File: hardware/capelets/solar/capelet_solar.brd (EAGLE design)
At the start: 54.6 x 40.5 mm, 4 parts

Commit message: hardware: updated capelets
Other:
- board text added: "SHEPHERD v1.4 CAPELET SOLAR"
- board text removed: "+"
- board text removed: "-"
- board text removed: "SHEPHERD v1.3 CAPELET SOLAR"
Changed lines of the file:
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@@
 <?xml version="1.0" encoding="utf-8"?>
 <!DOCTYPE eagle SYSTEM "eagle.dtd">
-<eagle version="9.3.2">
+<eagle version="9.4.2">
 <drawing>
 <settings>
@@
 <board>
 <plain>
-<text x="9.398" y="43.053" size="1.778" layer="25" font="vector" ratio="15">SHEPHERD v1.3 CAPELET SOLAR</text>
-<text x="9.652" y="1.27" size="1.778" layer="25" font="vector" ratio="15">+</text>
-<text x="4.572" y="1.397" size="1.778" layer="25" font="vector" ratio="15">-</text>
+<text x="8.001" y="42.418" size="1.905" layer="29" font="vector" ratio="17">SHEPHERD v1.4 CAPELET SOLAR</text>
 <dimension x1="0" y1="45.847" x2="54.61" y2="45.847" x3="27.305" y3="50.8" textsize="1.778" layer="47"/>
 <dimension x1="54.61" y1="45.72" x2="54.61" y2="5.207" x3="64.135" y3="25.4635" textsize="1.143" textratio="16" layer="47"/>

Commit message: hardware: fancy frames around capelet schematics
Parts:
- ROC1: value (none) -> 8M
- ROC2: value (none) -> 2M
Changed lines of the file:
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@@
 </autorouter>
 <elements>
-<element name="ROC2" library="mylib" package="RESC2012X65" value="" x="25.781" y="29.337" smashed="yes" rot="R180">
+<element name="ROC2" library="mylib" package="RESC2012X65" value="2M" x="25.781" y="29.337" smashed="yes" rot="R180">
 <attribute name="NAME" x="27.305" y="31.877" size="1.27" layer="25" font="vector" ratio="15" rot="R180"/>
 <attribute name="VALUE" x="28.0416" y="29.972" size="1.27" layer="27" ratio="10" rot="R180"/>
 </element>
-<element name="ROC1" library="mylib" package="RESC2012X65" value="" x="29.591" y="29.337" smashed="yes" rot="R180">
+<element name="ROC1" library="mylib" package="RESC2012X65" value="8M" x="29.591" y="29.337" smashed="yes" rot="R180">
 <attribute name="NAME" x="32.131" y="31.877" size="1.27" layer="25" font="vector" ratio="15" rot="R180"/>
 <attribute name="VALUE" x="31.8516" y="29.972" size="1.27" layer="27" ratio="10" rot="R180"/>

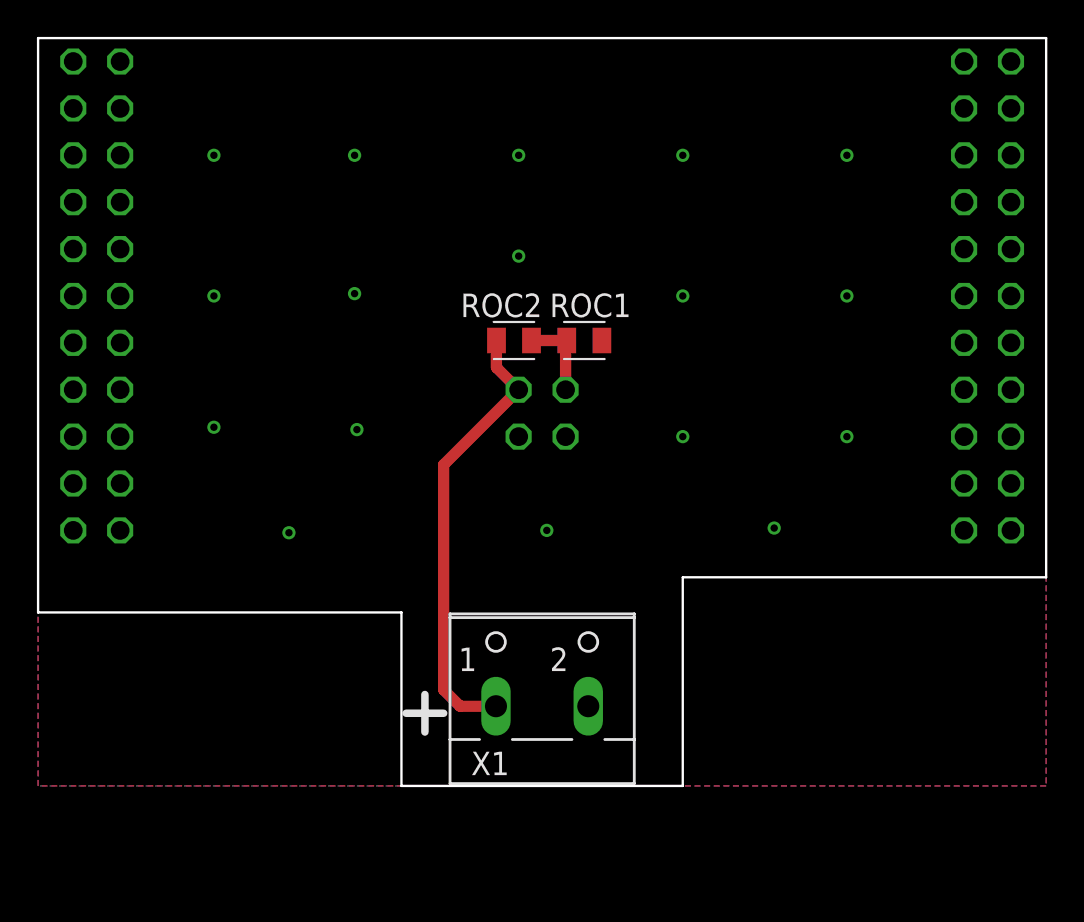
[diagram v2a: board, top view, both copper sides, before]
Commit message: hardware: prepared capelets for external manufacturing
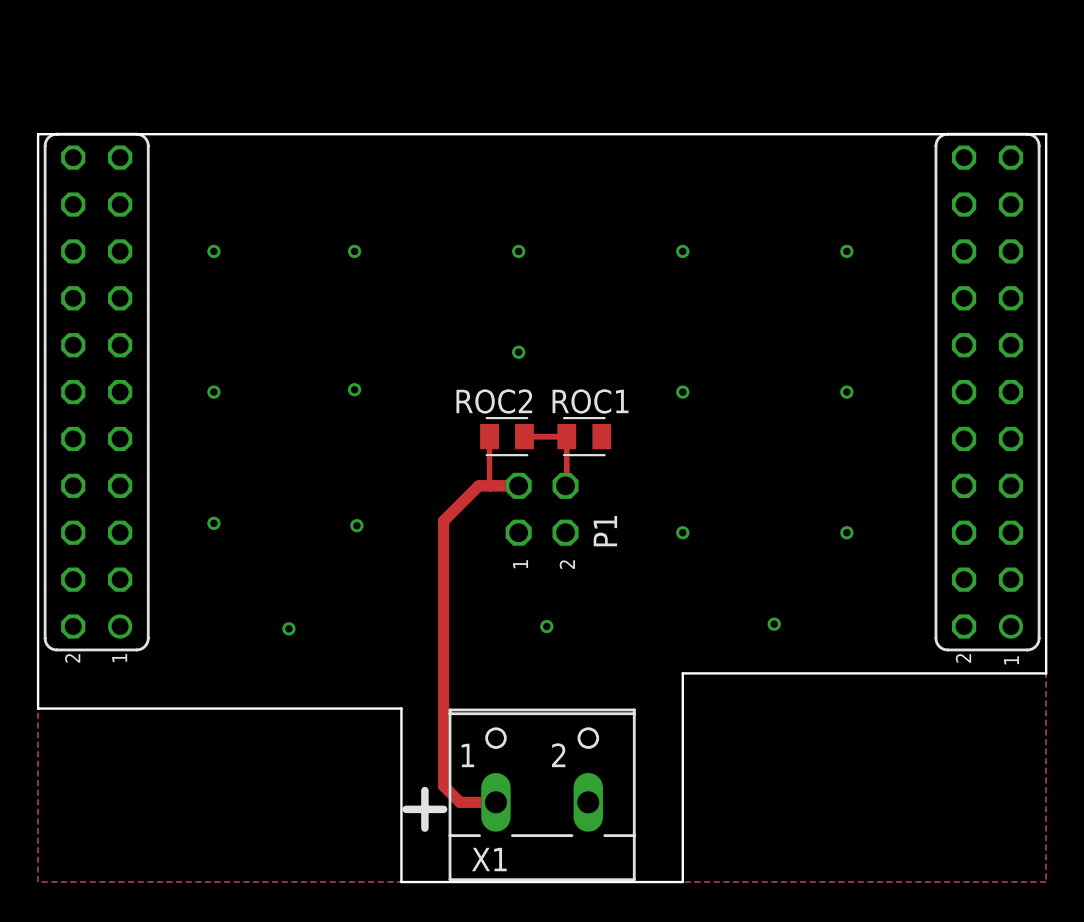
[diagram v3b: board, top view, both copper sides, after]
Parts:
- added P1: (no value), pinhead:2X02
- added P8, P9: FE11-2, shepherd:FE11-2
- U$1: value SHPRD_CPLT_H -> (none)
- moved ROC2 5.22 mm to (25.4, 24.1)
- moved ROC1 5.21 mm to (29.6, 24.1)
- moved X1 5.21 mm to (27.3, 5.59)
- moved U$1 0.64 mm to (0.00, 0.00)
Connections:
- removed net N$3: ROC1.2, ROC2.1, U$1.P1$4
- removed net SYS_5V: U$1.P9$7, U$1.P9$8
- removed net VDD_3V3: U$1.P9$3, U$1.P9$4
- removed net VDD_5V: U$1.P9$5, U$1.P9$6
- new net N$5: P1.4, ROC1.2, ROC2.1
- net GND: now also P1.1, P1.2; no longer U$1.P1$1, U$1.P1$3, U$1.P8$1, U$1.P8$2, U$1.P9$1, U$1.P9$2
- net N$2: now also P1.3; no longer U$1.P1$2
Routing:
- net N$5: track 0.00 -> 4.98 mm
- net N$3: track 4.60 -> 0.00 mm
- net N$2: track 24.3 -> 25.1 mm
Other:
- board text added: "1"
- board text added: "2"
- board text added: "P1: Pins pointing to bottom, solder on top"
- board text added: "SHEPHERD v1.5 CAPELET SOLAR"
- board text removed: "SHEPHERD v1.4 CAPELET SOLAR"
